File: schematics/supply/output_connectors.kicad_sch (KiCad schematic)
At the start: 24 parts, among them J17 banana jack + fuse 12A, J18 banana jack + fuse 12A, J19 Conn_02x04_Odd_Even, J20 jst xh angle, J21 jst xh angle, Q10 IRLML0030, Q10 IRLML5203, U6 INA3221

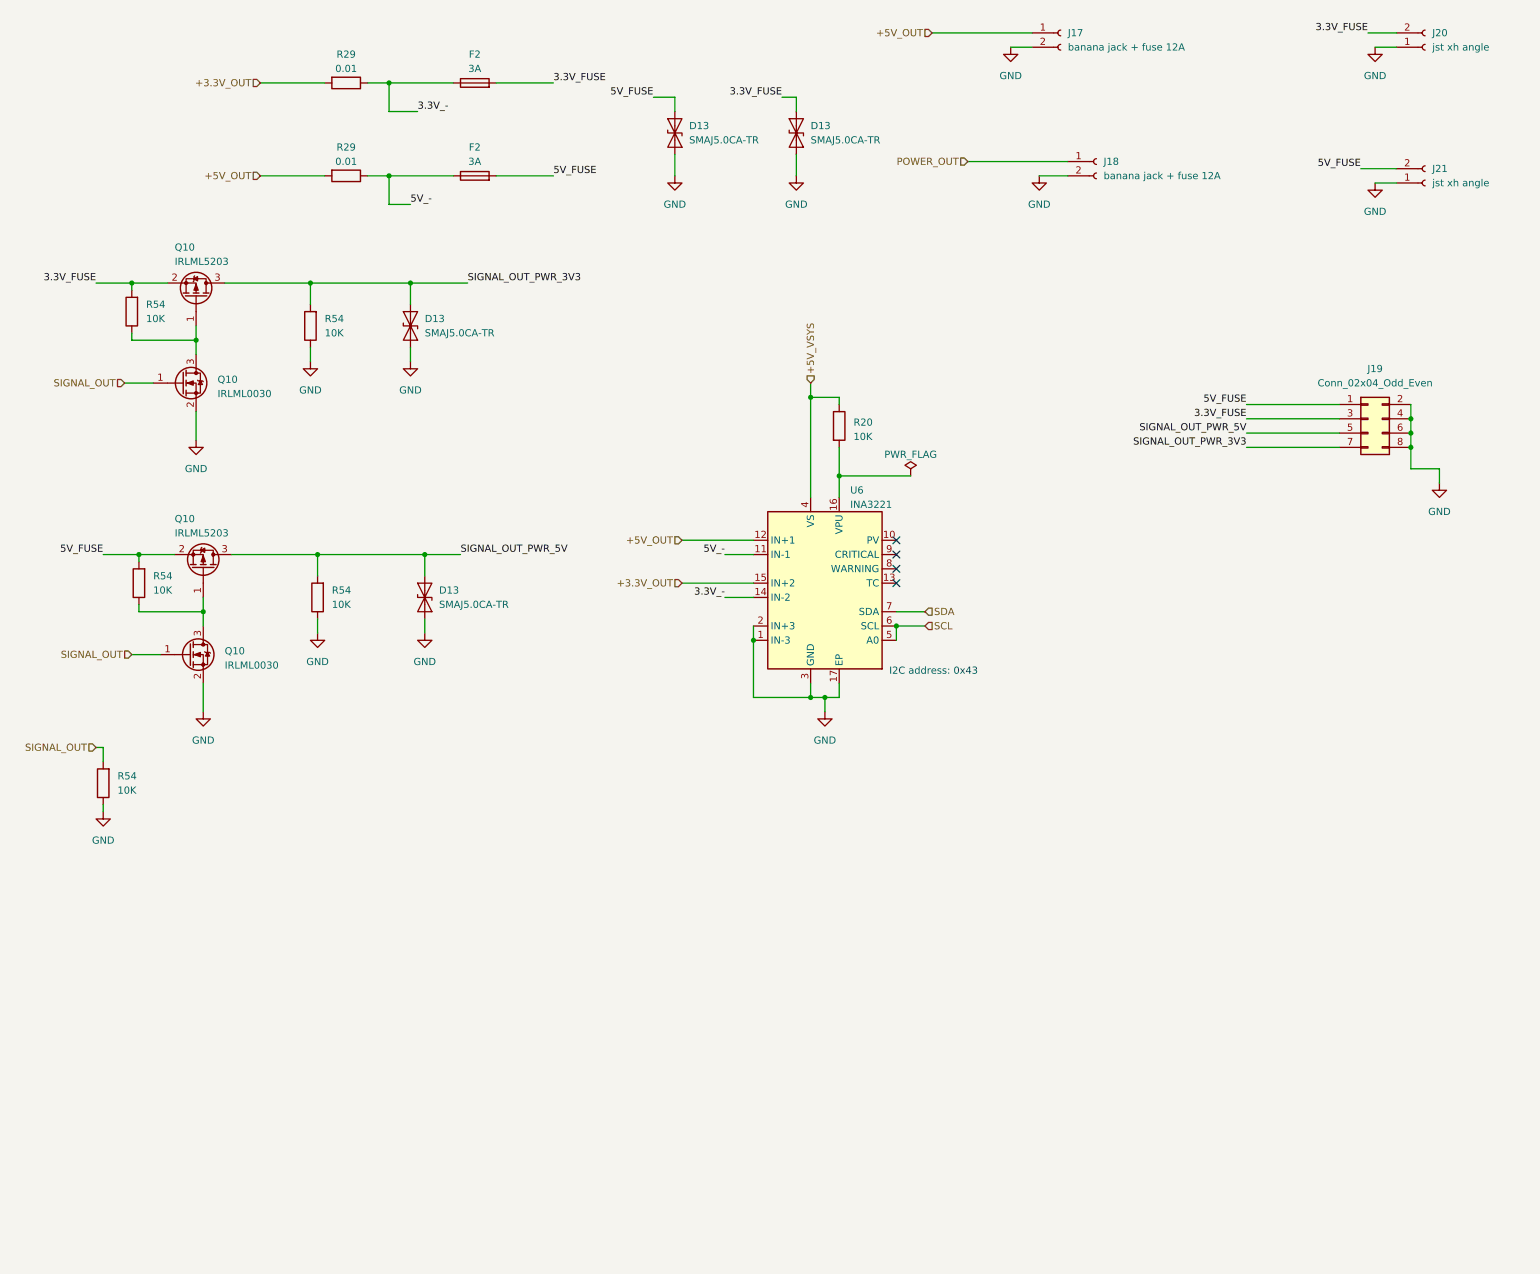
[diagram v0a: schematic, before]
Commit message: Changed fuse on 400V line
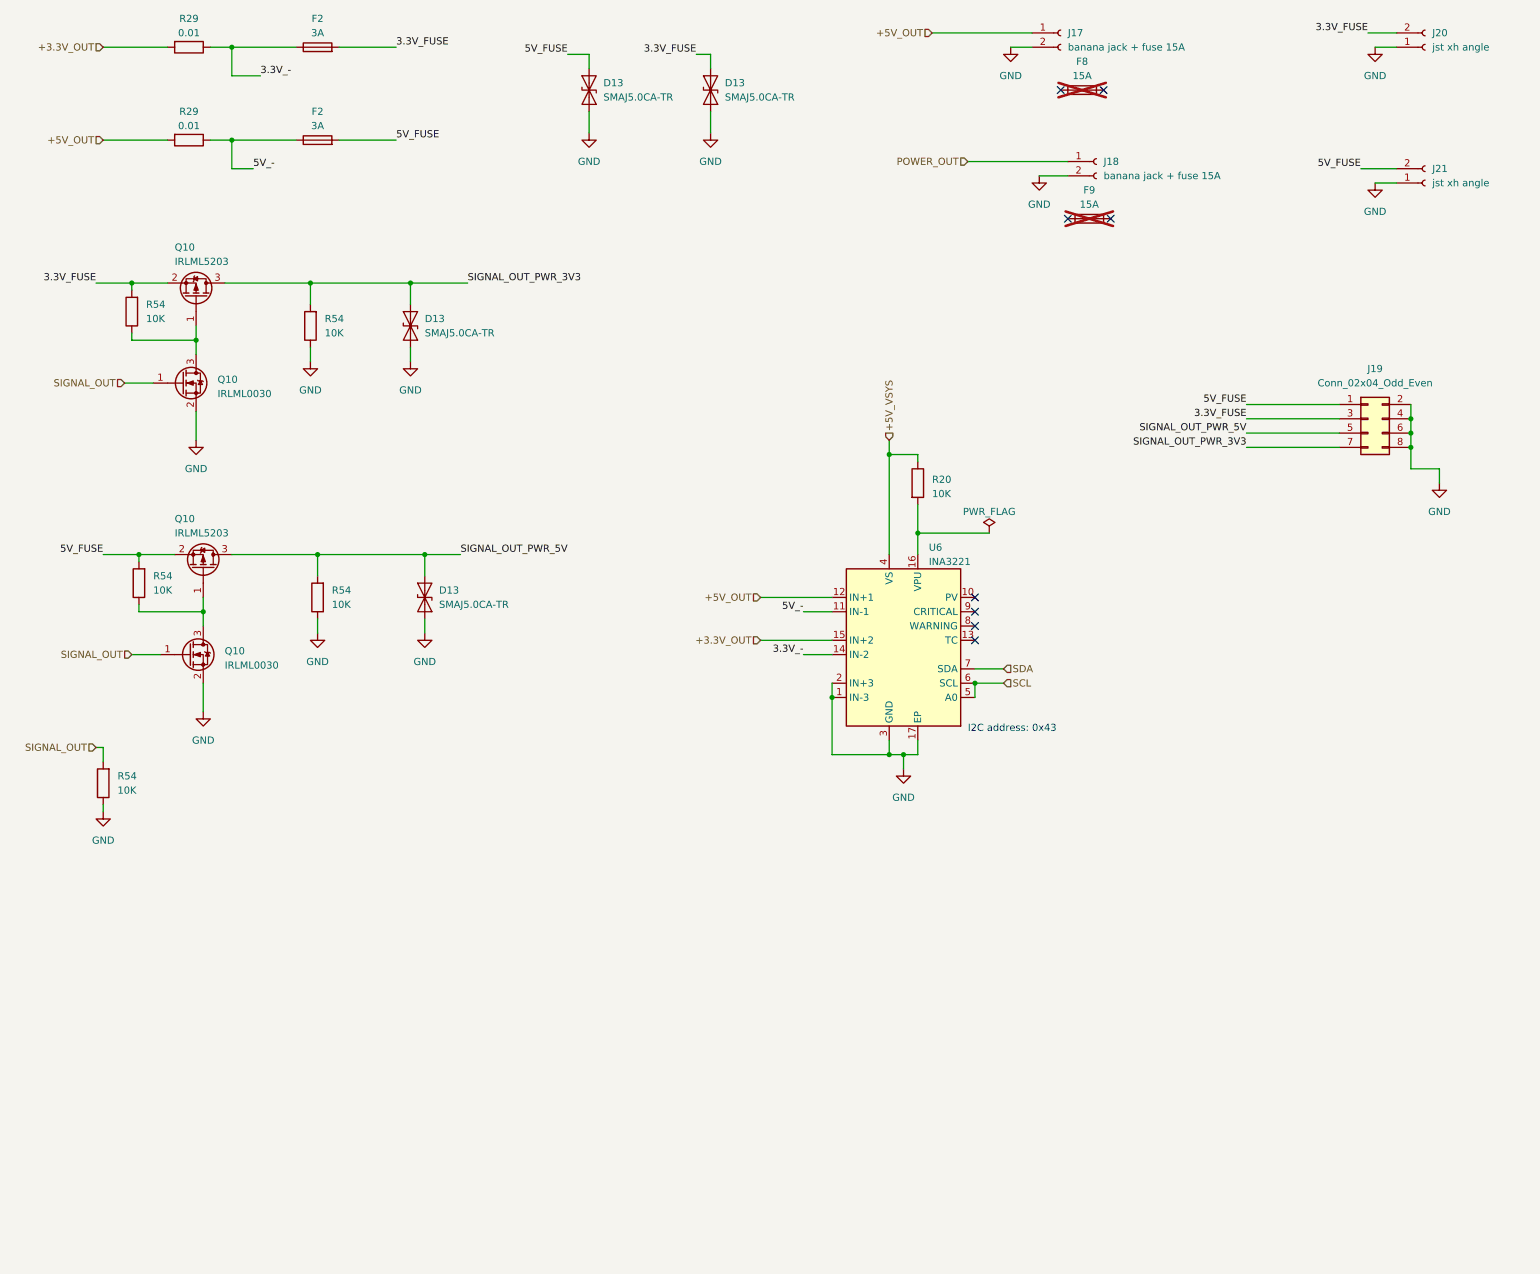
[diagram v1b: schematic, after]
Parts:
- added F8, F9: 15A, symbol Device:Fuse
- J17, J18: value banana jack + fuse 12A -> banana jack + fuse 15A
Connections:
- no-connect marks 4 -> 8
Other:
- moved on the sheet: D13, F2, R20, R29, U6

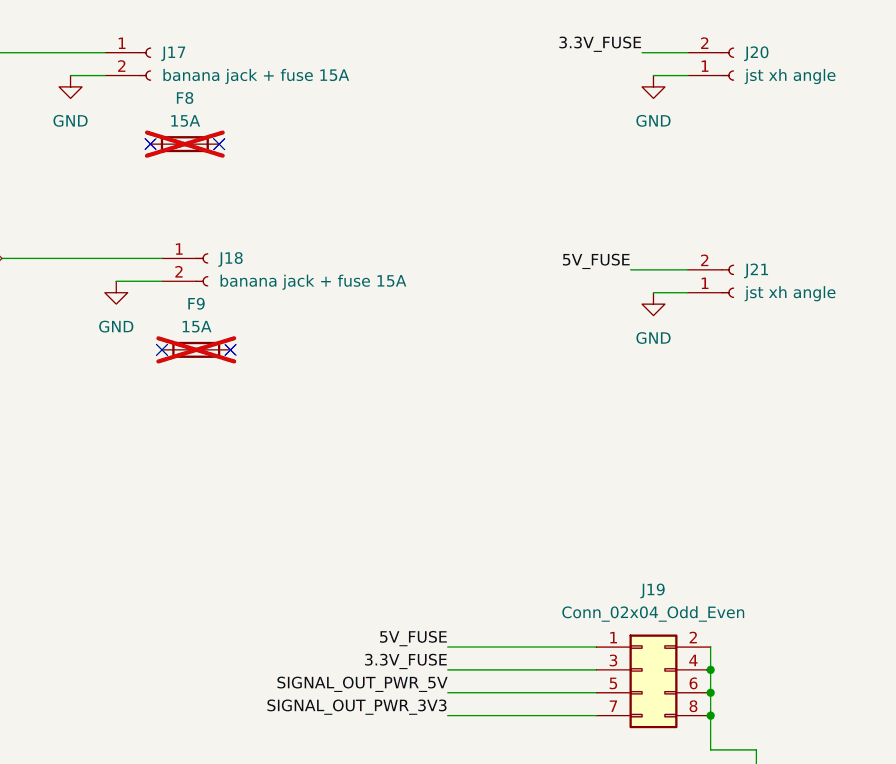
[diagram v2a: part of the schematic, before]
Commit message: UV board size changed to 100x100 to reduce production price
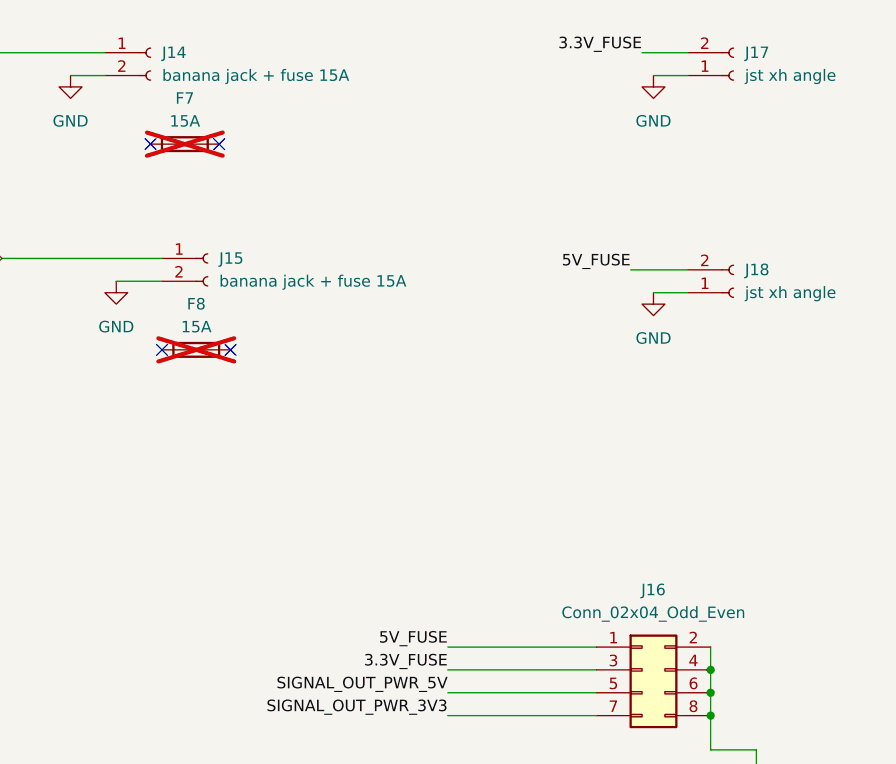
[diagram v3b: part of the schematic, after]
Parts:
- renumbered F8 to F7, F9 to F8, J17 to J14, J18 to J15, J19 to J16, J20 to J17, J21 to J18
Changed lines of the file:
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@@
         )
         (path "/1e139717-fcd1-4008-a6ea-4c993845e928/39d9543b-2a42-4758-87e9-56ce3e85ea36"
-          (reference "D29") (unit 1)
+          (reference "D23") (unit 1)
         )
       )
@@
         )
         (path "/1e139717-fcd1-4008-a6ea-4c993845e928/39d9543b-2a42-4758-87e9-56ce3e85ea36"
-          (reference "R73") (unit 1)
+          (reference "R55") (unit 1)
         )
       )
@@
         )
         (path "/1e139717-fcd1-4008-a6ea-4c993845e928/39d9543b-2a42-4758-87e9-56ce3e85ea36"
-          (reference "R79") (unit 1)
+          (reference "R61") (unit 1)
         )
       )
@@
   (symbol (lib_id "Device:Fuse") (at 205.74 29.21 90) (unit 1)
     (in_bom yes) (on_board no) (dnp yes) (fields_autoplaced)
-    (property "Reference" "F8" (at 205.74 24.13 90)
+    (property "Reference" "F7" (at 205.74 24.13 90)
       (effects (font (size 1.27 1.27)))
     )
@@
       (project "supply"
         (path "/1e139717-fcd1-4008-a6ea-4c993845e928/39d9543b-2a42-4758-87e9-56ce3e85ea36"
-          (reference "F8") (unit 1)
+          (reference "F7") (unit 1)
         )
       )
@@
         )
         (path "/1e139717-fcd1-4008-a6ea-4c993845e928/39d9543b-2a42-4758-87e9-56ce3e85ea36"
-          (reference "R77") (unit 1)
+          (reference "R59") (unit 1)
         )
       )
@@
   (symbol (lib_id "Connector:Conn_01x02_Socket") (at 266.7 45.72 0) (mirror x) (unit 1)
     (in_bom yes) (on_board yes) (dnp no)
-    (property "Reference" "J21" (at 267.97 43.18 0)
+    (property "Reference" "J18" (at 267.97 43.18 0)
       (effects (font (size 1.27 1.27)) (justify left))
     )
@@
       (project "supply"
         (path "/1e139717-fcd1-4008-a6ea-4c993845e928/39d9543b-2a42-4758-87e9-56ce3e85ea36"
-          (reference "J21") (unit 1)
+          (reference "J18") (unit 1)
         )
       )
@@
         )
         (path "/1e139717-fcd1-4008-a6ea-4c993845e928/39d9543b-2a42-4758-87e9-56ce3e85ea36"
-          (reference "R76") (unit 1)
+          (reference "R58") (unit 1)
         )
       )
@@
         )
         (path "/1e139717-fcd1-4008-a6ea-4c993845e928/39d9543b-2a42-4758-87e9-56ce3e85ea36"
-          (reference "#FLG019") (unit 1)
+          (reference "#FLG014") (unit 1)
         )
       )
@@
   (symbol (lib_id "Connector:Conn_01x02_Socket") (at 201.93 19.05 0) (unit 1)
     (in_bom yes) (on_board yes) (dnp no) (fields_autoplaced)
-    (property "Reference" "J17" (at 203.2 19.05 0)
+    (property "Reference" "J14" (at 203.2 19.05 0)
       (effects (font (size 1.27 1.27)) (justify left))
     )
@@
       (project "supply"
         (path "/1e139717-fcd1-4008-a6ea-4c993845e928/39d9543b-2a42-4758-87e9-56ce3e85ea36"
-          (reference "J17") (unit 1)
+          (reference "J14") (unit 1)
         )
       )
@@
         )
         (path "/1e139717-fcd1-4008-a6ea-4c993845e928/39d9543b-2a42-4758-87e9-56ce3e85ea36"
-          (reference "R78") (unit 1)
+          (reference "R60") (unit 1)
         )
       )
@@
   (symbol (lib_id "Connector:Conn_01x02_Socket") (at 266.7 21.59 0) (mirror x) (unit 1)
     (in_bom yes) (on_board yes) (dnp no)
-    (property "Reference" "J20" (at 267.97 19.05 0)
+    (property "Reference" "J17" (at 267.97 19.05 0)
       (effects (font (size 1.27 1.27)) (justify left))
     )
@@
       (project "supply"
         (path "/1e139717-fcd1-4008-a6ea-4c993845e928/39d9543b-2a42-4758-87e9-56ce3e85ea36"
-          (reference "J20") (unit 1)
+          (reference "J17") (unit 1)
         )
       )
@@
         )
         (path "/1e139717-fcd1-4008-a6ea-4c993845e928/39d9543b-2a42-4758-87e9-56ce3e85ea36"
-          (reference "R75") (unit 1)
+          (reference "R57") (unit 1)
         )
       )
@@
         )
         (path "/1e139717-fcd1-4008-a6ea-4c993845e928/39d9543b-2a42-4758-87e9-56ce3e85ea36"
-          (reference "Q12") (unit 1)
+          (reference "Q10") (unit 1)
         )
       )
@@
         )
         (path "/1e139717-fcd1-4008-a6ea-4c993845e928/39d9543b-2a42-4758-87e9-56ce3e85ea36"
-          (reference "Q14") (unit 1)
+          (reference "Q12") (unit 1)
         )
       )
@@
         )
         (path "/1e139717-fcd1-4008-a6ea-4c993845e928/39d9543b-2a42-4758-87e9-56ce3e85ea36"
-          (reference "R74") (unit 1)
+          (reference "R56") (unit 1)
         )
       )
@@
         )
         (path "/1e139717-fcd1-4008-a6ea-4c993845e928/39d9543b-2a42-4758-87e9-56ce3e85ea36"
-          (reference "U25") (unit 1)
+          (reference "U20") (unit 1)
         )
       )
@@
         )
         (path "/1e139717-fcd1-4008-a6ea-4c993845e928/39d9543b-2a42-4758-87e9-56ce3e85ea36"
-          (reference "Q13") (unit 1)
+          (reference "Q11") (unit 1)
         )
       )
@@
         )
         (path "/1e139717-fcd1-4008-a6ea-4c993845e928/39d9543b-2a42-4758-87e9-56ce3e85ea36"
-          (reference "D32") (unit 1)
+          (reference "D26") (unit 1)
         )
       )
@@
   (symbol (lib_id "Connector:Conn_01x02_Socket") (at 208.28 41.91 0) (unit 1)
     (in_bom yes) (on_board yes) (dnp no) (fields_autoplaced)
-    (property "Reference" "J18" (at 209.55 41.91 0)
+    (property "Reference" "J15" (at 209.55 41.91 0)
       (effects (font (size 1.27 1.27)) (justify left))
     )
@@
       (project "supply"
         (path "/1e139717-fcd1-4008-a6ea-4c993845e928/39d9543b-2a42-4758-87e9-56ce3e85ea36"
-          (reference "J18") (unit 1)
+          (reference "J15") (unit 1)
         )
       )
@@
         )
         (path "/1e139717-fcd1-4008-a6ea-4c993845e928/39d9543b-2a42-4758-87e9-56ce3e85ea36"
-          (reference "Q11") (unit 1)
+          (reference "Q9") (unit 1)
         )
       )
@@
         )
         (path "/1e139717-fcd1-4008-a6ea-4c993845e928/39d9543b-2a42-4758-87e9-56ce3e85ea36"
-          (reference "R72") (unit 1)
+          (reference "R54") (unit 1)
         )
       )
@@
         )
         (path "/1e139717-fcd1-4008-a6ea-4c993845e928/39d9543b-2a42-4758-87e9-56ce3e85ea36"
-          (reference "D30") (unit 1)
+          (reference "D24") (unit 1)
         )
       )
@@
         )
         (path "/1e139717-fcd1-4008-a6ea-4c993845e928/39d9543b-2a42-4758-87e9-56ce3e85ea36"
-          (reference "D31") (unit 1)
+          (reference "D25") (unit 1)
         )
       )
@@
         )
         (path "/1e139717-fcd1-4008-a6ea-4c993845e928/39d9543b-2a42-4758-87e9-56ce3e85ea36"
-          (reference "F7") (unit 1)
+          (reference "F6") (unit 1)
         )
       )
@@
   (symbol (lib_id "Connector_Generic:Conn_02x04_Odd_Even") (at 256.54 87.63 0) (unit 1)
     (in_bom yes) (on_board yes) (dnp no) (fields_autoplaced)
-    (property "Reference" "J19" (at 257.81 78.74 0)
+    (property "Reference" "J16" (at 257.81 78.74 0)
       (effects (font (size 1.27 1.27)))
     )
@@
       (project "supply"
         (path "/1e139717-fcd1-4008-a6ea-4c993845e928/39d9543b-2a42-4758-87e9-56ce3e85ea36"
-          (reference "J19") (unit 1)
+          (reference "J16") (unit 1)
         )
       )
@@
   (symbol (lib_id "Device:Fuse") (at 207.01 52.07 90) (unit 1)
     (in_bom yes) (on_board no) (dnp yes) (fields_autoplaced)
-    (property "Reference" "F9" (at 207.01 46.99 90)
+    (property "Reference" "F8" (at 207.01 46.99 90)
       (effects (font (size 1.27 1.27)))
     )
@@
       (project "supply"
         (path "/1e139717-fcd1-4008-a6ea-4c993845e928/39d9543b-2a42-4758-87e9-56ce3e85ea36"
-          (reference "F9") (unit 1)
+          (reference "F8") (unit 1)
         )
       )
@@
         )
         (path "/1e139717-fcd1-4008-a6ea-4c993845e928/39d9543b-2a42-4758-87e9-56ce3e85ea36"
-          (reference "F6") (unit 1)
-        )
-      )
+          (reference "F5") (unit 1)
+        )
+      )
